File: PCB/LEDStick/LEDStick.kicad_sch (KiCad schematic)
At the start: 27 parts, among them J1 Conn_01x04_Pin

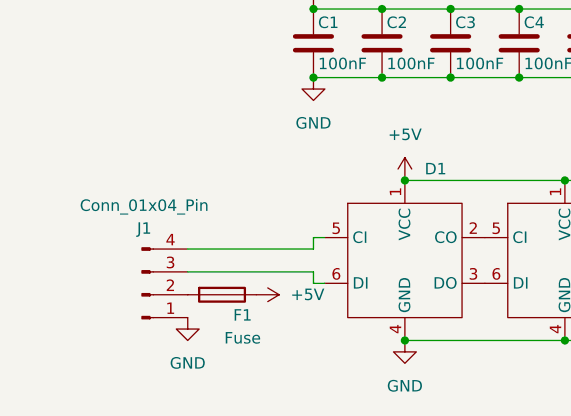
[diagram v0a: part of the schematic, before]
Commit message: main layout complete needs headers and testpoints
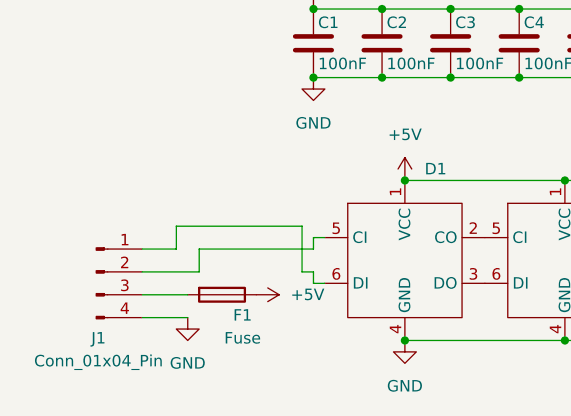
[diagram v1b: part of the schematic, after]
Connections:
- net GND: now also J1.4 (Pin_4); no longer J1.1 (Pin_1)
- net at J1.2 (Pin_2): now also D1.5 (CI); no longer F1.2
- net at D1.6 (DI): now also J1.1 (Pin_1); no longer J1.3 (Pin_3)
- new net: F1.2, J1.3 (Pin_3)
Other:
- moved on the sheet: J1
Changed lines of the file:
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@@
 	(wire
 		(pts
-			(xy 93.98 91.44) (xy 80.01 91.44)
+			(xy 92.71 91.44) (xy 93.98 91.44)
 		)
 		(stroke
@@
 	(wire
 		(pts
+			(xy 78.74 88.9) (xy 78.74 86.36)
+		)
+		(stroke
+			(width 0)
+			(type default)
+		)
+	)
+	(wire
+		(pts
+			(xy 93.98 88.9) (xy 81.28 88.9)
+		)
+		(stroke
+			(width 0)
+			(type default)
+		)
+	)
+	(wire
+		(pts
 			(xy 95.25 92.71) (xy 93.98 92.71)
 		)
@@
 	(wire
 		(pts
+			(xy 92.71 86.36) (xy 92.71 91.44)
+		)
+		(stroke
+			(width 0)
+			(type default)
+		)
+	)
+	(wire
+		(pts
 			(xy 116.84 69.85) (xy 124.46 69.85)
 		)
@@
 	(wire
 		(pts
+			(xy 74.93 88.9) (xy 78.74 88.9)
+		)
+		(stroke
+			(width 0)
+			(type default)
+		)
+	)
+	(wire
+		(pts
 			(xy 93.98 62.23) (xy 101.6 62.23)
 		)
@@
 	(wire
 		(pts
-			(xy 93.98 88.9) (xy 80.01 88.9)
-		)
-		(stroke
-			(width 0)
-			(type default)
-		)
-	)
-	(wire
-		(pts
 			(xy 299.72 99.06) (xy 317.5 99.06)
 		)
@@
 	(wire
 		(pts
+			(xy 81.28 91.44) (xy 74.93 91.44)
+		)
+		(stroke
+			(width 0)
+			(type default)
+		)
+	)
+	(wire
+		(pts
+			(xy 81.28 88.9) (xy 81.28 91.44)
+		)
+		(stroke
+			(width 0)
+			(type default)
+		)
+	)
+	(wire
+		(pts
 			(xy 406.4 99.06) (xy 424.18 99.06)
 		)
@@
 	(wire
 		(pts
+			(xy 74.93 96.52) (xy 80.01 96.52)
+		)
+		(stroke
+			(width 0)
+			(type default)
+		)
+	)
+	(wire
+		(pts
 			(xy 93.98 69.85) (xy 101.6 69.85)
 		)
@@
 	(wire
 		(pts
+			(xy 74.93 93.98) (xy 80.01 93.98)
+		)
+		(stroke
+			(width 0)
+			(type default)
+		)
+	)
+	(wire
+		(pts
 			(xy 157.48 99.06) (xy 175.26 99.06)
 		)
@@
 		(pts
 			(xy 210.82 81.28) (xy 228.6 81.28)
+		)
+		(stroke
+			(width 0)
+			(type default)
+		)
+	)
+	(wire
+		(pts
+			(xy 78.74 86.36) (xy 92.71 86.36)
 		)
 		(stroke
@@
 	(symbol
 		(lib_id "Connector:Conn_01x04_Pin")
-		(at 74.93 93.98 0)
-		(mirror x)
+		(at 69.85 91.44 0)
 		(unit 1)
 		(exclude_from_sim no)
@@
 		(dnp no)
 		(property "Reference" "J1"
-			(at 75.184 86.614 0)
+			(at 70.104 98.806 0)
 			(effects
 				(font
@@
 		)
 		(property "Value" "Conn_01x04_Pin"
-			(at 75.184 84.074 0)
+			(at 70.104 101.346 0)
 			(effects
 				(font
@@
 		)
 		(property "Footprint" "Danger_Doughnut_Lib:JST_S04B-PASK-2_LF__SN_"
-			(at 74.93 93.98 0)
+			(at 69.85 91.44 0)
 			(effects
 				(font
@@
 		)
 		(property "Datasheet" "~"
-			(at 74.93 93.98 0)
+			(at 69.85 91.44 0)
 			(effects
 				(font
@@
 		)
 		(property "Description" "Generic connector, single row, 01x04, script generated"
-			(at 74.93 93.98 0)
-			(effects
-				(font
+			(at 69.85 91.44 0)
+			(effects
+				(font
